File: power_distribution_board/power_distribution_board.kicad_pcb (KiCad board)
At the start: 2 copper layers, 67 parts, among them J1 CONN_01x03, J10 CONN_02X01, J11 CONN_02X01, J12 CONN_02X01, J13 CONN_02X01, J14 CONN_02X01, J15 CONN_02X01, J16 CONN_02X01, J17 CONN_02X01, J18 CONN_02X01, J19 CONN_02X01, J2 CONN_02X01, J20 CONN_02X01, J21 CONN_02X01, J22 CONN_02X01, J23 CONN_02X01, J3 CONN_02X01, J4 CONN_02X01, J5 CONN_02X01, J6 CONN_02X01, J7 CONN_02X01, J8 CONN_02X01, J9 CONN_02X01, Q1 NMOS_SSSGD, Q2 NMOS_SSSGD, Q3 NMOS_SSSGD, Q4 NMOS_SSSGD, Q5 Q_NMOS_GSD, U1 EHHD015A0A, U2 LTC1473, U3 EHHD010A0B, U4 LM317EMP, U5 BTS6133D, U6 A1120

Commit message: a few more things routed
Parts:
- moved TP3 21.8 mm to (238.8, 119.6)
- moved D4 20.8 mm to (242.7, 120.7), turned to 90 degrees
- moved R10 16.9 mm to (219.4, 110.4)
- moved R3 16.6 mm to (242.7, 116.8), turned to 270 degrees
- moved Q5 10.2 mm to (220.2, 114.2), turned to 90 degrees
- moved C7 6.02 mm to (226.8, 113.7)
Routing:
- net Net-(Q5-Pad3): track 0.00 -> 28.1 mm
- net /PWR_SWITCHED: track 2.71 -> 9.01 mm
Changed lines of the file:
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@@
   (general
     (links 201)
-    (no_connects 117)
-    (area 0 0 0 0)
+    (no_connects 114)
+    (area -58.975 -44.695 245.322 152.609762)
     (thickness 1.6)
     (drawings 0)
-    (tracks 101)
+    (tracks 113)
     (zones 0)
     (modules 67)
@@
   )
   (module Capacitors_SMD:C_1210 (layer F.Cu)
-    (at 222.8 118.2 270)
+    (at 226.7585 113.665 270)
     (descr "Capacitor SMD 1210, reflow soldering, AVX (see smccp.pdf)")
     (tags "capacitor 1210")
     (attr smd)
-    (fp_text reference C7 (at 0 -2.25 270) (layer F.SilkS)
+    (fp_text reference C7 (at 3.2258 -0.1143 360) (layer F.SilkS)
       (effects (font (size 1 1) (thickness 0.15)))
     )
-    (fp_text value 100μ (at 0 2.5 270) (layer F.Fab)
+    (fp_text value 100μ (at -3.2258 -0.0127 360) (layer F.Fab)
       (effects (font (size 1 1) (thickness 0.15)))
     )
-    (fp_text user %R (at 0 -2.25 270) (layer F.Fab)
+    (fp_text user %R (at 3.2258 -0.1143 360) (layer F.Fab)
       (effects (font (size 1 1) (thickness 0.15)))
     )
@@
   )
   (module LEDs:LED_0805 (layer F.Cu)
-    (at 238.78 100.26)
+    (at 242.697 120.7135 90)
     (descr "LED 0805 smd package")
     (tags "LED led 0805 SMD smd SMT smt smdled SMDLED smtled SMTLED")
     (attr smd)
-    (fp_text reference D4 (at 0 -1.45) (layer F.SilkS)
+    (fp_text reference D4 (at 0 -1.45 90) (layer F.SilkS)
       (effects (font (size 1 1) (thickness 0.15)))
     )
-    (fp_text value LED (at 0 1.55) (layer F.Fab)
+    (fp_text value LED (at 0 1.55 90) (layer F.Fab)
       (effects (font (size 1 1) (thickness 0.15)))
     )
@@
     (fp_line (start -1.95 0.85) (end -1.95 -0.85) (layer F.CrtYd) (width 0.05))
     (fp_line (start -1.95 -0.85) (end 1.95 -0.85) (layer F.CrtYd) (width 0.05))
-    (pad 2 smd rect (at 1.1 0 180) (size 1.2 1.2) (layers F.Cu F.Paste F.Mask)
+    (pad 2 smd rect (at 1.1 0 270) (size 1.2 1.2) (layers F.Cu F.Paste F.Mask)
       (net 10 "Net-(D4-Pad2)"))
-    (pad 1 smd rect (at -1.1 0 180) (size 1.2 1.2) (layers F.Cu F.Paste F.Mask)
+    (pad 1 smd rect (at -1.1 0 270) (size 1.2 1.2) (layers F.Cu F.Paste F.Mask)
       (net 2 GND))
     (model ${KISYS3DMOD}/LEDs.3dshapes/LED_0805.wrl
@@
   )
   (module TO_SOT_Packages_SMD:SOT-23 (layer F.Cu)
-    (at 215.1 105.3)
+    (at 220.1545 114.173 90)
     (descr "SOT-23, Standard")
     (tags SOT-23)
     (attr smd)
-    (fp_text reference Q5 (at 0 -2.5) (layer F.SilkS)
+    (fp_text reference Q5 (at 0 -2.5 90) (layer F.SilkS)
       (effects (font (size 1 1) (thickness 0.15)))
     )
-    (fp_text value Q_NMOS_GSD (at 0 2.5) (layer F.Fab)
+    (fp_text value Q_NMOS_GSD (at -2.794 0 180) (layer F.Fab) hide
       (effects (font (size 1 1) (thickness 0.15)))
     )
-    (fp_text user %R (at 0 0 90) (layer F.Fab)
+    (fp_text user %R (at 0 0 180) (layer F.Fab)
       (effects (font (size 0.5 0.5) (thickness 0.075)))
     )
@@
     (fp_line (start 0.76 -1.58) (end -1.4 -1.58) (layer F.SilkS) (width 0.12))
     (fp_line (start 0.76 1.58) (end -0.7 1.58) (layer F.SilkS) (width 0.12))
-    (pad 1 smd rect (at -1 -0.95) (size 0.9 0.8) (layers F.Cu F.Paste F.Mask)
+    (pad 1 smd rect (at -1 -0.95 90) (size 0.9 0.8) (layers F.Cu F.Paste F.Mask)
       (net 27 /PWR_ENABLE))
-    (pad 2 smd rect (at -1 0.95) (size 0.9 0.8) (layers F.Cu F.Paste F.Mask)
+    (pad 2 smd rect (at -1 0.95 90) (size 0.9 0.8) (layers F.Cu F.Paste F.Mask)
       (net 2 GND))
-    (pad 3 smd rect (at 1 0) (size 0.9 0.8) (layers F.Cu F.Paste F.Mask)
+    (pad 3 smd rect (at 1 0 90) (size 0.9 0.8) (layers F.Cu F.Paste F.Mask)
       (net 28 "Net-(Q5-Pad3)"))
     (model ${KISYS3DMOD}/TO_SOT_Packages_SMD.3dshapes/SOT-23.wrl
@@
   )
   (module Resistors_SMD:R_0603 (layer F.Cu)
-    (at 243.86 100.26)
+    (at 242.697 116.7765 270)
     (descr "Resistor SMD 0603, reflow soldering, Vishay (see dcrcw.pdf)")
     (tags "resistor 0603")
     (attr smd)
-    (fp_text reference R3 (at 0 -1.45) (layer F.SilkS)
+    (fp_text reference R3 (at 0 -1.45 270) (layer F.SilkS)
       (effects (font (size 1 1) (thickness 0.15)))
     )
-    (fp_text value 8.2k (at 0 1.5) (layer F.Fab)
+    (fp_text value 8.2k (at 0 1.5 270) (layer F.Fab)
       (effects (font (size 1 1) (thickness 0.15)))
     )
-    (fp_text user %R (at 0 0) (layer F.Fab)
+    (fp_text user %R (at 0 0 270) (layer F.Fab)
       (effects (font (size 0.4 0.4) (thickness 0.075)))
     )
@@
     (fp_line (start 1.25 0.7) (end 1.25 -0.7) (layer F.CrtYd) (width 0.05))
     (fp_line (start 1.25 0.7) (end -1.25 0.7) (layer F.CrtYd) (width 0.05))
-    (pad 1 smd rect (at -0.75 0) (size 0.5 0.9) (layers F.Cu F.Paste F.Mask)
+    (pad 1 smd rect (at -0.75 0 270) (size 0.5 0.9) (layers F.Cu F.Paste F.Mask)
       (net 17 /20V_PWR))
-    (pad 2 smd rect (at 0.75 0) (size 0.5 0.9) (layers F.Cu F.Paste F.Mask)
+    (pad 2 smd rect (at 0.75 0 270) (size 0.5 0.9) (layers F.Cu F.Paste F.Mask)
       (net 10 "Net-(D4-Pad2)"))
     (model ${KISYS3DMOD}/Resistors_SMD.3dshapes/R_0603.wrl
@@
   )
   (module Resistors_SMD:R_0603 (layer F.Cu)
-    (at 223.52 93.98)
+    (at 219.4052 110.3884)
     (descr "Resistor SMD 0603, reflow soldering, Vishay (see dcrcw.pdf)")
     (tags "resistor 0603")
@@
   )
   (module agg_lib:TESTPAD (layer F.Cu)
-    (at 248.94 100.26)
+    (at 238.76 119.5705)
     (fp_text reference TP3 (at 0 -1.4) (layer F.Fab) hide
       (effects (font (size 1 1) (thickness 0.15)))
@@
   (segment (start 57.09 139.3825) (end 55.1325 139.3825) (width 0.2) (layer F.Cu) (net 4))
   (segment (start 55.1325 139.3825) (end 55 139.25) (width 0.2) (layer F.Cu) (net 4))
+  (segment (start 239.6 113.7) (end 233.3 113.7) (width 0.2) (layer F.Cu) (net 5))
   (segment (start 160.8 124.45) (end 160.95 124.3) (width 0.2) (layer F.Cu) (net 5))
   (segment (start 160.95 124.3) (end 163.45 124.3) (width 0.2) (layer F.Cu) (net 5))
-  (segment (start 166.6 130.2) (end 166.25 130.55) (width 0.4) (layer F.Cu) (net 6) (status C00000))
-  (segment (start 166.25 130.55) (end 160.3 130.55) (width 0.4) (layer F.Cu) (net 6) (status C00000))
+  (segment (start 166.6 130.2) (end 166.25 130.55) (width 0.4) (layer F.Cu) (net 6))
+  (segment (start 166.25 130.55) (end 160.3 130.55) (width 0.4) (layer F.Cu) (net 6))
   (segment (start 165.15 127.1) (end 166.6 127.1) (width 0.4) (layer F.Cu) (net 6))
   (segment (start 166.6 127.1) (end 166.6 127) (width 0.4) (layer F.Cu) (net 6))
@@
   (segment (start 163.45 122) (end 163 121.55) (width 0.2) (layer F.Cu) (net 6))
   (segment (start 163 121.55) (end 160.6 121.55) (width 0.2) (layer F.Cu) (net 6) (status 20))
-  (segment (start 156.7 134) (end 156.7 132.05) (width 0.2) (layer F.Cu) (net 12) (status C00000))
+  (segment (start 156.7 134) (end 156.7 132.05) (width 0.2) (layer F.Cu) (net 12))
   (segment (start 57 132.25) (end 57.25 132.25) (width 0.2) (layer F.Cu) (net 13))
   (segment (start 57.25 132.25) (end 57.75 131.75) (width 0.2) (layer F.Cu) (net 13))
@@
   (segment (start 64.75 140.75) (end 62.3875 140.75) (width 0.2) (layer F.Cu) (net 26))
   (segment (start 62.3875 140.75) (end 62.29 140.6525) (width 0.2) (layer F.Cu) (net 26))
-  (segment (start 156.7 130.55) (end 156.7 128.6) (width 0.2) (layer F.Cu) (net 27) (status C00000))
-  (segment (start 156.7 130.55) (end 158.2 132.05) (width 0.2) (layer F.Cu) (net 27) (status 400000))
-  (segment (start 158.2 132.05) (end 160.3 132.05) (width 0.2) (layer F.Cu) (net 27) (status 800000))
-  (segment (start 166.6 132.74) (end 165.91 132.05) (width 0.2) (layer F.Cu) (net 27) (status C00000))
-  (segment (start 165.91 132.05) (end 160.3 132.05) (width 0.2) (layer F.Cu) (net 27) (status C00000))
+  (segment (start 156.7 130.55) (end 156.7 128.6) (width 0.2) (layer F.Cu) (net 27))
+  (segment (start 156.7 130.55) (end 158.2 132.05) (width 0.2) (layer F.Cu) (net 27))
+  (segment (start 158.2 132.05) (end 160.3 132.05) (width 0.2) (layer F.Cu) (net 27))
+  (segment (start 166.6 132.74) (end 165.91 132.05) (width 0.2) (layer F.Cu) (net 27))
+  (segment (start 165.91 132.05) (end 160.3 132.05) (width 0.2) (layer F.Cu) (net 27))
+  (segment (start 220.1545 113.173) (end 220.1545 110.3891) (width 0.2) (layer F.Cu) (net 28) (status C00000))
+  (segment (start 220.1545 110.3891) (end 220.1552 110.3884) (width 0.2) (layer F.Cu) (net 28) (status C00000))
+  (segment (start 238.1692 114.84) (end 239.6 114.84) (width 0.2) (layer F.Cu) (net 28))
+  (segment (start 237.236 115.7732) (end 238.1692 114.84) (width 0.2) (layer F.Cu) (net 28))
+  (segment (start 237.236 116.9924) (end 237.236 115.7732) (width 0.2) (layer F.Cu) (net 28))
+  (segment (start 236.3216 117.9068) (end 237.236 116.9924) (width 0.2) (layer F.Cu) (net 28))
+  (segment (start 229.4128 117.9068) (end 236.3216 117.9068) (width 0.2) (layer F.Cu) (net 28))
+  (segment (start 229.1588 117.6528) (end 229.4128 117.9068) (width 0.2) (layer F.Cu) (net 28))
+  (segment (start 229.1588 114.3) (end 229.1588 117.6528) (width 0.2) (layer F.Cu) (net 28))
+  (segment (start 228.0318 113.173) (end 229.1588 114.3) (width 0.2) (layer F.Cu) (net 28))
+  (segment (start 220.1545 113.173) (end 228.0318 113.173) (width 0.2) (layer F.Cu) (net 28))
   (segment (start 55.25 137.4775) (end 54.7725 137) (width 0.2) (layer F.Cu) (net 29))
   (segment (start 54.7725 137) (end 53 137) (width 0.2) (layer F.Cu) (net 29))

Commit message: finish pdb
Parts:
- added G***: LOGO, cauv_lib:LOGO, F.Cu at (87.6, 138.9)
- moved C5 245.1 mm to (171.2, 132.8), turned to 0 degrees
- moved C4 245.0 mm to (149.9, 106.4), turned to 270 degrees
- moved U3 210.4 mm to (177.3, 101.6), turned to 90 degrees
- moved J2 192.6 mm to (197.9, 122.0), turned to 90 degrees
- moved U1 188.7 mm to (118.2, 97.2), turned to 180 degrees
- moved J3 181.4 mm to (197.9, 114.0), turned to 90 degrees
- moved J12 173.3 mm to (179.3, 139.2)
- moved J13 173.3 mm to (187.3, 139.2)
- moved J14 173.3 mm to (195.3, 139.2)
- moved J15 173.3 mm to (203.3, 139.2)
- moved J4 170.3 mm to (197.9, 106.0), turned to 90 degrees
- moved D2 169.8 mm to (183.8, 67.8), turned to 180 degrees
- moved TP1 159.3 mm to (84.6, 104.8), turned to 180 degrees
- moved J5 159.2 mm to (197.9, 98.0), turned to 90 degrees
- moved R1 157.1 mm to (84.6, 100.1), turned to 90 degrees
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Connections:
- U1 pad 1: GND -> /PWR_SWITCHED
- U1 pad 3: /PWR_SWITCHED -> GND
- U3 pad 1: GND -> /PWR_SWITCHED
- U3 pad 3: /PWR_SWITCHED -> GND
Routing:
- net /PWR_ENABLE: track 12.8 -> 90.9 mm, vias 0 -> 1
- net GND: track 0.00 -> 43.1 mm, vias 0 -> 12
- net /AO_PWR: track 21.7 -> 48.6 mm
- net Net-(C2-Pad1): track 4.25 -> 23.6 mm
- net Net-(D2-Pad2): track 0.00 -> 7.80 mm
- net Net-(D1-Pad2): track 0.00 -> 7.55 mm
- net /5V_PWR: track 0.00 -> 3.95 mm
- net Net-(Q1-Pad1): track 0.00 -> 3.47 mm
- net Net-(D4-Pad2): track 0.00 -> 2.90 mm
- net Net-(Q4-Pad4): track 7.74 -> 10.4 mm, vias 0 -> 2
- net Net-(Q3-Pad1): track 0.00 -> 1.66 mm
- net Net-(Q1-Pad4): track 6.79 -> 8.05 mm, vias 0 -> 2
- net Net-(Q3-Pad4): track 6.91 -> 8.03 mm
- net Net-(Q2-Pad4): track 13.7 -> 14.0 mm, vias 0 -> 2
- net Net-(R9-Pad2): track 21.2 -> 21.3 mm, vias 0 -> 2
- added copper zone on F.Cu, net /12V_PWR
- added copper zone on F.Cu, net /20V_PWR
- added copper zone on F.Cu, net /5V_PWR
- added copper zone on F.Cu, net /PWR_SWITCHED
- added copper zone on F.Cu, net BATT1
- added copper zone on F.Cu, net BATT2
- added copper zone on B.Cu, net GND
- added copper zone on F.Cu, net Net-(Q1-Pad1)
- added copper zone on F.Cu, net Net-(Q2-Pad5)
- added copper zone on F.Cu, net Net-(Q3-Pad1)
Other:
- board outline added: 130 x 90 mm
- board text added: "12V Supply"
- board text added: "20V Supply"
- board text added: "5V Supply"
- board text added: "Motors"
- board text added: "PDB v0.1"

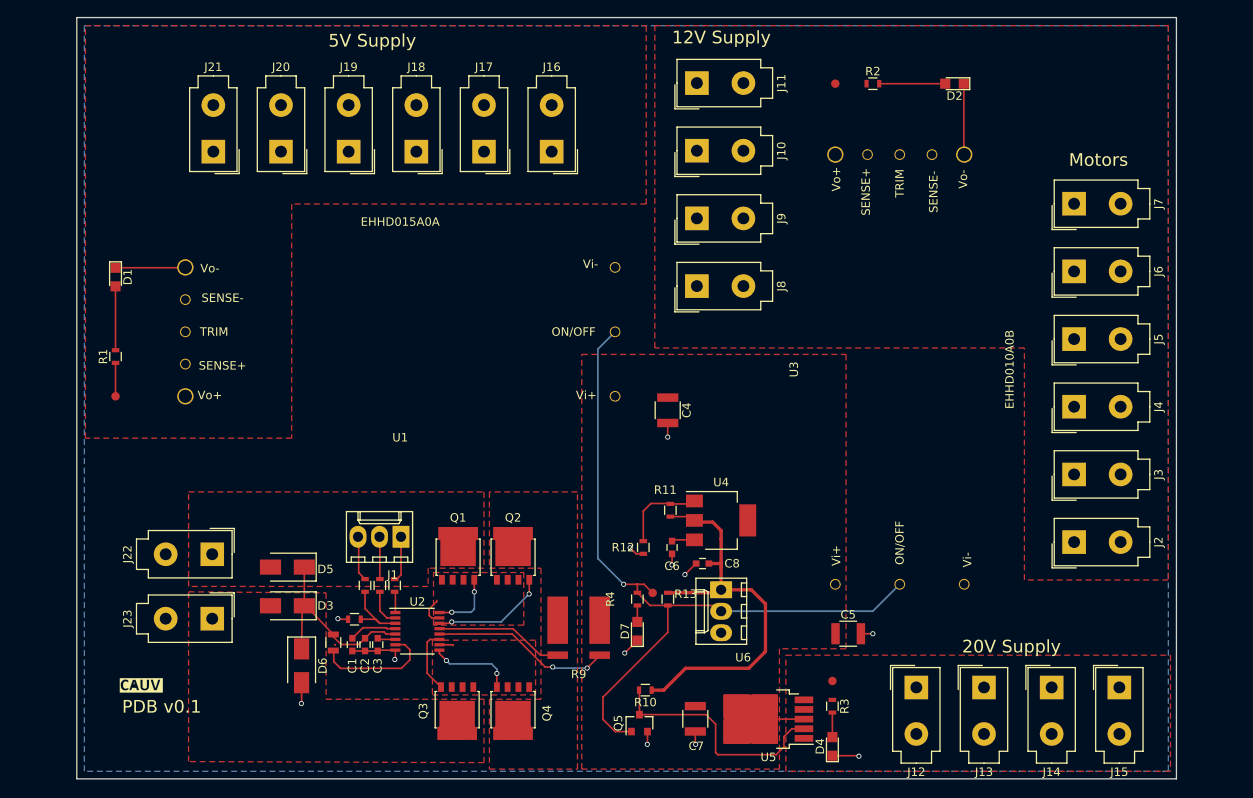
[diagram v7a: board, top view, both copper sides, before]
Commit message: added mounting holes and changed light board footprints
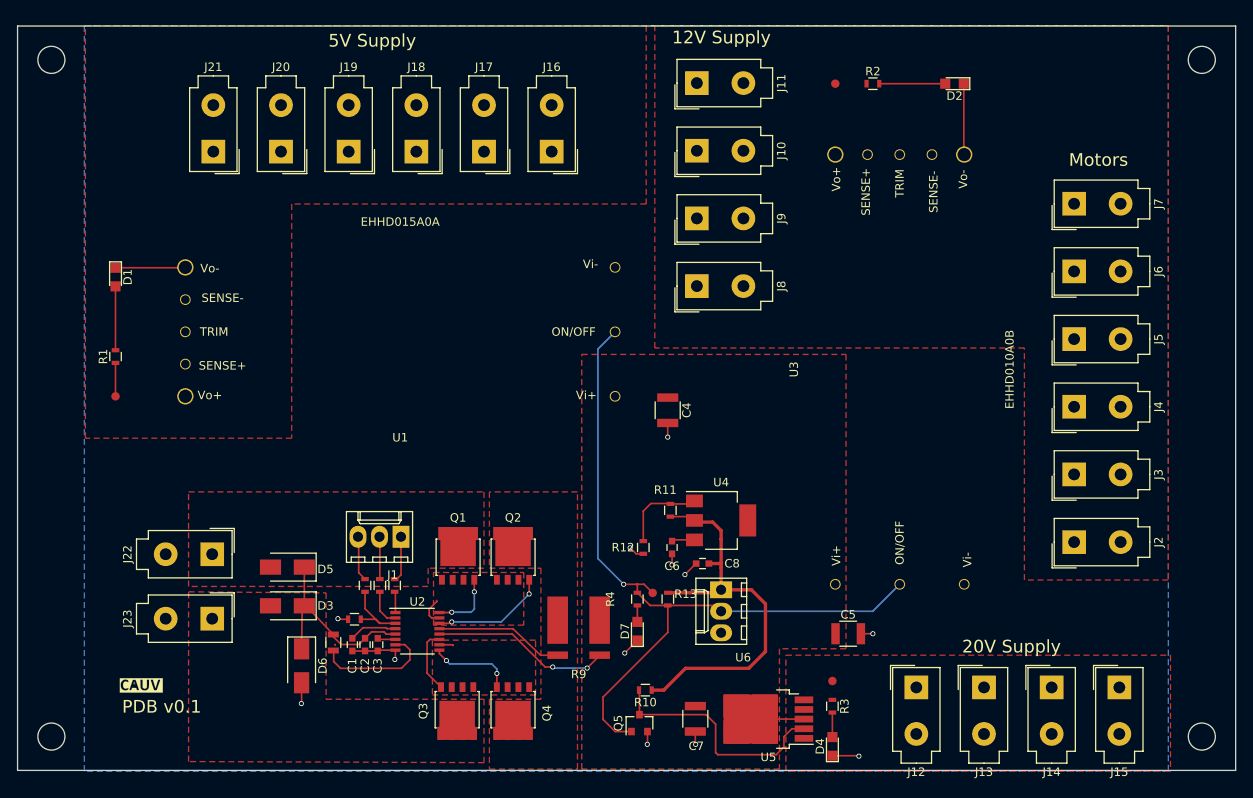
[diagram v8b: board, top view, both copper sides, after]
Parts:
- added ?: , Mounting_Holes:MountingHole_3.2mm_M3, F.Cu at (213.0, 65.0)
- added ?: , Mounting_Holes:MountingHole_3.2mm_M3, F.Cu at (213.0, 145.0)
- added ?: , Mounting_Holes:MountingHole_3.2mm_M3, F.Cu at (77.0, 145.0)
- added ?: , Mounting_Holes:MountingHole_3.2mm_M3, F.Cu at (77.0, 65.0)
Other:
- board size 130 x 90 mm -> 144 x 88 mm
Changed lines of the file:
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@@
 (kicad_pcb (version 4) (host pcbnew 4.0.6)
   (general
-    (links 201)
+    (links 0)
     (no_connects 0)
-    (area 79.924999 59.924999 210.075001 150.075001)
+    (area 79.924999 59.924999 210.075001 150.267)
     (thickness 1.6)
     (drawings 9)
     (tracks 224)
     (zones 0)
-    (modules 68)
+    (modules 72)
     (nets 38)
   )
@@
       (xy -0.794329 -0.385252)) (layer F.SilkS) (width 0.01))
   )
+  (module Mounting_Holes:MountingHole_3.2mm_M3 (layer F.Cu)
+    (at 213 65)
+    (descr "Mounting Hole 3.2mm, no annular, M3")
+    (tags "mounting hole 3.2mm no annular m3")
+    (attr virtual)
+    (fp_text reference "" (at 0 -4.2) (layer F.SilkS)
+      (effects (font (size 1 1) (thickness 0.15)))
+    )
+    (fp_text value "" (at 0 4.2) (layer F.Fab)
+      (effects (font (size 1 1) (thickness 0.15)))
+    )
+    (fp_text user %R (at 0.3 0) (layer F.Fab)
+      (effects (font (size 1 1) (thickness 0.15)))
+    )
+    (fp_circle (center 0 0) (end 3.2 0) (layer Cmts.User) (width 0.15))
+    (fp_circle (center 0 0) (end 3.45 0) (layer F.CrtYd) (width 0.05))
+    (pad 1 np_thru_hole circle (at 0 0) (size 3.2 3.2) (drill 3.2) (layers *.Cu *.Mask))
+  )
+  (module Mounting_Holes:MountingHole_3.2mm_M3 (layer F.Cu)
+    (at 213 145)
+    (descr "Mounting Hole 3.2mm, no annular, M3")
+    (tags "mounting hole 3.2mm no annular m3")
+    (attr virtual)
+    (fp_text reference "" (at 0 -4.2) (layer F.SilkS)
+      (effects (font (size 1 1) (thickness 0.15)))
+    )
+    (fp_text value "" (at 0 4.2) (layer F.Fab)
+      (effects (font (size 1 1) (thickness 0.15)))
+    )
+    (fp_text user %R (at 0.3 0) (layer F.Fab)
+      (effects (font (size 1 1) (thickness 0.15)))
+    )
+    (fp_circle (center 0 0) (end 3.2 0) (layer Cmts.User) (width 0.15))
+    (fp_circle (center 0 0) (end 3.45 0) (layer F.CrtYd) (width 0.05))
+    (pad 1 np_thru_hole circle (at 0 0) (size 3.2 3.2) (drill 3.2) (layers *.Cu *.Mask))
+  )
+  (module Mounting_Holes:MountingHole_3.2mm_M3 (layer F.Cu)
+    (at 77 145)
+    (descr "Mounting Hole 3.2mm, no annular, M3")
+    (tags "mounting hole 3.2mm no annular m3")
+    (attr virtual)
+    (fp_text reference "" (at 0 -4.2) (layer F.SilkS)
+      (effects (font (size 1 1) (thickness 0.15)))
+    )
+    (fp_text value "" (at 0 4.2) (layer F.Fab)
+      (effects (font (size 1 1) (thickness 0.15)))
+    )
+    (fp_text user %R (at 0.3 0) (layer F.Fab)
+      (effects (font (size 1 1) (thickness 0.15)))
+    )
+    (fp_circle (center 0 0) (end 3.2 0) (layer Cmts.User) (width 0.15))
+    (fp_circle (center 0 0) (end 3.45 0) (layer F.CrtYd) (width 0.05))
+    (pad 1 np_thru_hole circle (at 0 0) (size 3.2 3.2) (drill 3.2) (layers *.Cu *.Mask))
+  )
+  (module Mounting_Holes:MountingHole_3.2mm_M3 (layer F.Cu)
+    (at 77 65)
+    (descr "Mounting Hole 3.2mm, no annular, M3")
+    (tags "mounting hole 3.2mm no annular m3")
+    (attr virtual)
+    (fp_text reference "" (at 0 -4.2) (layer F.SilkS)
+      (effects (font (size 1 1) (thickness 0.15)))
+    )
+    (fp_text value "" (at 0 4.2) (layer F.Fab)
+      (effects (font (size 1 1) (thickness 0.15)))
+    )
+    (fp_text user %R (at 0.3 0) (layer F.Fab)
+      (effects (font (size 1 1) (thickness 0.15)))
+    )
+    (fp_circle (center 0 0) (end 3.2 0) (layer Cmts.User) (width 0.15))
+    (fp_circle (center 0 0) (end 3.45 0) (layer F.CrtYd) (width 0.05))
+    (pad 1 np_thru_hole circle (at 0 0) (size 3.2 3.2) (drill 3.2) (layers *.Cu *.Mask))
+  )
+  (gr_line (start 73 149) (end 73 61) (layer Edge.Cuts) (width 0.15))
+  (gr_line (start 217 149) (end 73 149) (layer Edge.Cuts) (width 0.15))
+  (gr_line (start 217 61) (end 217 149) (layer Edge.Cuts) (width 0.15))
+  (gr_line (start 73 61) (end 217 61) (layer Edge.Cuts) (width 0.15))
   (gr_text "20V Supply" (at 190.5 134.366) (layer F.SilkS)
     (effects (font (size 1.5 1.5) (thickness 0.3)))
@@
     (effects (font (size 1.5 1.5) (thickness 0.3)))
   )
-  (gr_line (start 210 150) (end 80 150) (angle 90) (layer Edge.Cuts) (width 0.15))
-  (gr_line (start 210 60) (end 210 150) (angle 90) (layer Edge.Cuts) (width 0.15))
-  (gr_line (start 80 60) (end 210 60) (angle 90) (layer Edge.Cuts) (width 0.15))
-  (gr_line (start 80 60) (end 80 150) (angle 90) (layer Edge.Cuts) (width 0.15))
   (segment (start 110.5465 134.1501) (end 110.529 134.1326) (width 0.2) (layer F.Cu) (net 0) (status 30))
   (segment (start 110.5465 134.1501) (end 110.529 134.1326) (width 0.2) (layer F.Cu) (net 0) (status 30))
